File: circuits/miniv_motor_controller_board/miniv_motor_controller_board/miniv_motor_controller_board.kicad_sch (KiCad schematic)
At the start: 34 parts, among them J1 DC_in, J2 T200_ESC_power, J3 T200_ESC_signal, J4 Conn_EStop_Signal, Q1 2SC1815, Q2 2SC1815, U1 Teensy4.1, U2 TLP624, U3 TLP624

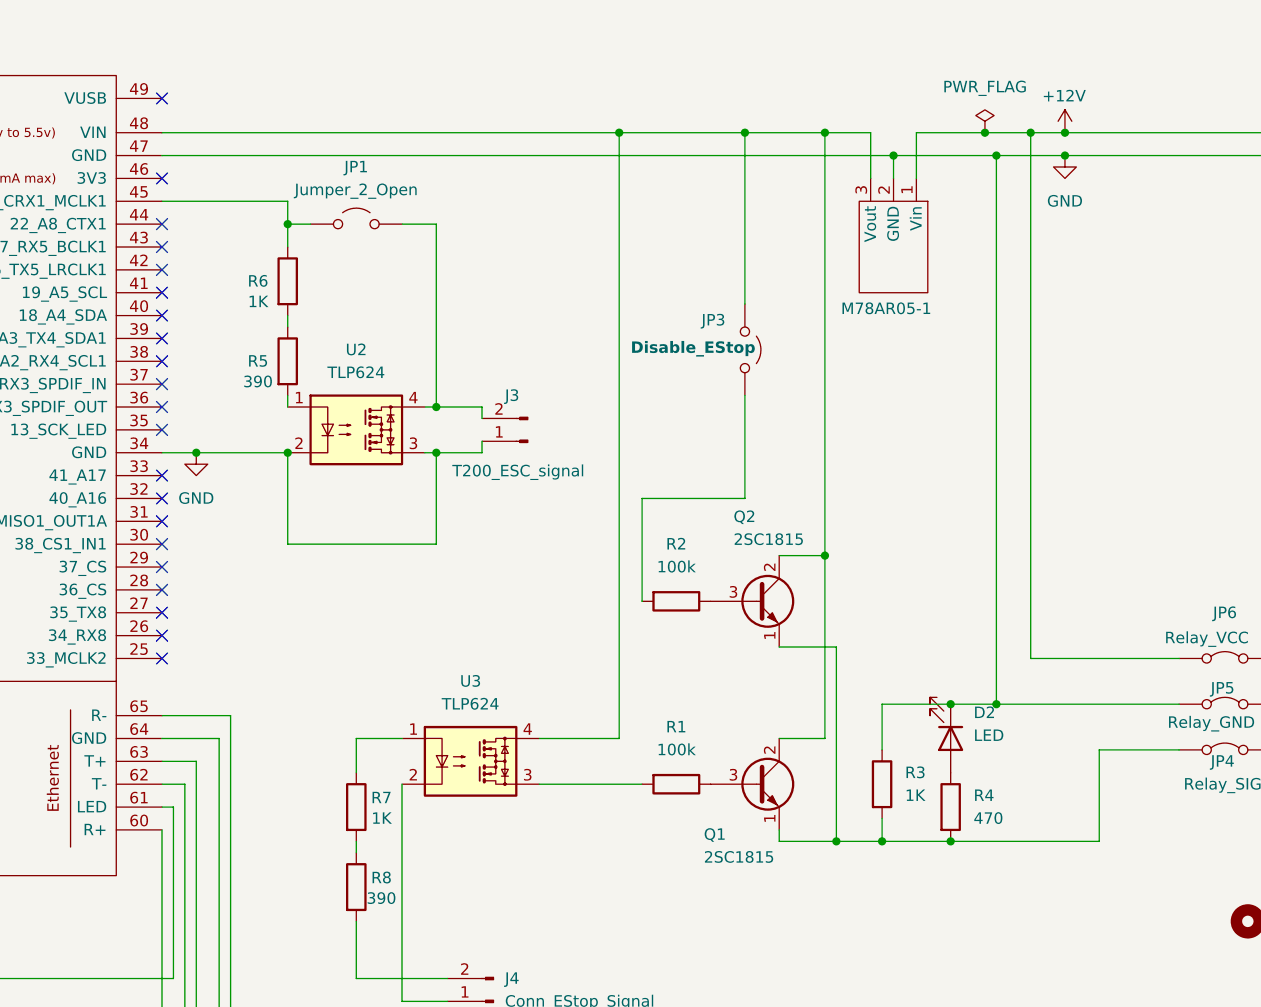
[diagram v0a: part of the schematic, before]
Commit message: add SS-12D00G3 and modify RJLD-260YC1
Signed-off-by: Masaya Kataoka <ms.kataoka@gmail.com>
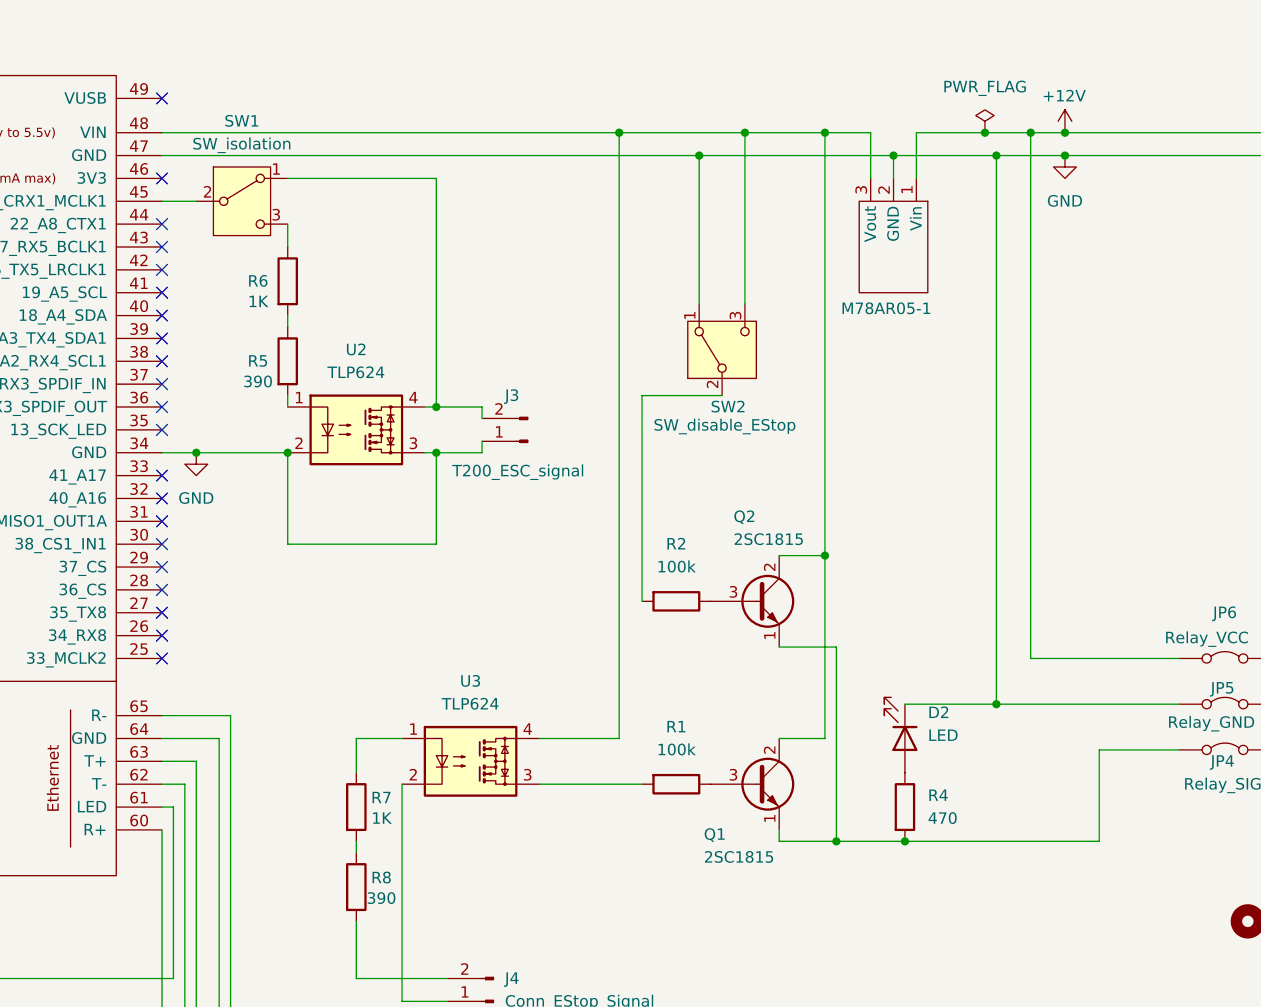
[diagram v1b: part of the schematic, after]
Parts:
- removed JP1: Jumper_2_Open, Connector_PinHeader_2.54mm:PinHeader_1x02_P2.54mm_Vertical, symbol Jumper:Jumper_2_Open
- removed JP3: Disable_EStop, Connector_PinHeader_2.54mm:PinHeader_1x02_P2.54mm_Vertical, symbol Jumper:Jumper_2_Open
- removed R3: 1K, Resistor_THT:R_Axial_DIN0207_L6.3mm_D2.5mm_P10.16mm_Horizontal, symbol Device:R
- added SW1: SW_isolation, SS-12D00G3:SS-12D00G3, symbol Switch:SW_SPDT
- added SW2: SW_disable_EStop, SS-12D00G3:SS-12D00G3, symbol Switch:SW_SPDT
- C1: footprint (none) -> Capacitor_THT:C_Disc_D5.1mm_W3.2mm_P5.00mm
- U5: footprint https://akizukidenshi.com/catalog/g/g129472/ -> RJLD-260YC1:RJLD-260YC1
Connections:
- net GND: now also SW2.1 (A)
- net at R6.1: now also SW1.3 (C); no longer U1.45 (23_A9_CRX1_MCLK1)
- net at J3.2 (Pin_2), U2.4: now also SW1.1 (A)
- net at M78AR05-1.3 (Vout), Q1.2 (C), Q2.2 (C)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: now also SW2.3 (C)
- net at R2.2: now also SW2.2 (B)
- net at U4. (VCC(CN1-1)): now also JP2.2 (B)
- new net: SW1.2 (B), U1.45 (23_A9_CRX1_MCLK1)
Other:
- moved on the sheet: D2, R4

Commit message: update board
Signed-off-by: Masaya Kataoka <ms.kataoka@gmail.com>
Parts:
- U1: footprint Teensy:Teensy41 -> Teensy_Custom:Teensy41
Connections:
- net GND: now also U1.1 (GND); no longer U1.47 (GND)
- net at U4. (VCC(CN1-1)): now also JP2.2 (B)
- net at SW1.2 (B): now also U1.33 (41_A17); no longer U1.45 (23_A9_CRX1_MCLK1)
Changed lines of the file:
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@@
 	)
 	(junction
-		(at 168.91 64.77)
+		(at 137.16 67.31)
 		(diameter 0)
 		(color 0 0 0 0)
 	)
 	(junction
-		(at 151.13 111.76)
+		(at 168.91 64.77)
 		(diameter 0)
 		(color 0 0 0 0)
 	)
 	(junction
-		(at 158.75 67.31)
+		(at 151.13 111.76)
 		(diameter 0)
 		(color 0 0 0 0)
 	)
 	(junction
-		(at 177.8 67.31)
+		(at 158.75 67.31)
 		(diameter 0)
 		(color 0 0 0 0)
 	)
 	(junction
-		(at 137.16 67.31)
+		(at 177.8 67.31)
 		(diameter 0)
 		(color 0 0 0 0)
@@
 	)
 	(no_connect
+		(at 77.47 72.39)
+	)
+	(no_connect
 		(at 21.59 69.85)
 	)
@@
 	)
 	(no_connect
-		(at 77.47 102.87)
+		(at 77.47 85.09)
 	)
 	(no_connect
-		(at 77.47 85.09)
+		(at 77.47 67.31)
 	)
 	(no_connect
@@
 	)
 	(no_connect
-		(at 21.59 64.77)
-	)
-	(no_connect
 		(at 21.59 118.11)
 	)
@@
 	(wire
 		(pts
-			(xy 78.74 158.75) (xy 78.74 139.7)
+			(xy 106.68 48.26) (xy 21.59 48.26)
 		)
 		(stroke
@@
 	(wire
 		(pts
-			(xy 77.47 180.34) (xy 46.99 180.34)
+			(xy 78.74 158.75) (xy 78.74 139.7)
 		)
 		(stroke
@@
 	(wire
 		(pts
-			(xy 152.4 143.51) (xy 160.02 143.51)
+			(xy 77.47 180.34) (xy 46.99 180.34)
 		)
 		(stroke
@@
 	(wire
 		(pts
-			(xy 107.95 100.33) (xy 113.03 100.33)
+			(xy 152.4 143.51) (xy 160.02 143.51)
 		)
 		(stroke
@@
 	(wire
 		(pts
-			(xy 156.21 64.77) (xy 156.21 69.85)
+			(xy 107.95 100.33) (xy 113.03 100.33)
 		)
 		(stroke
@@
 	(wire
 		(pts
-			(xy 77.47 72.39) (xy 81.28 72.39)
+			(xy 156.21 64.77) (xy 156.21 69.85)
 		)
 		(stroke
@@
 	(wire
 		(pts
+			(xy 85.09 102.87) (xy 77.47 102.87)
+		)
+		(stroke
+			(width 0)
+			(type default)
+		)
+	)
+	(wire
+		(pts
 			(xy 170.18 67.31) (xy 170.18 128.27)
 		)
@@
 	(wire
 		(pts
-			(xy 77.47 67.31) (xy 137.16 67.31)
+			(xy 81.28 82.55) (xy 85.09 82.55)
 		)
 		(stroke
@@
 	(wire
 		(pts
+			(xy 106.68 67.31) (xy 106.68 48.26)
+		)
+		(stroke
+			(width 0)
+			(type default)
+		)
+	)
+	(wire
+		(pts
 			(xy 177.8 64.77) (xy 260.35 64.77)
 		)
@@
 	(wire
 		(pts
+			(xy 81.28 72.39) (xy 81.28 82.55)
+		)
+		(stroke
+			(width 0)
+			(type default)
+		)
+	)
+	(wire
+		(pts
 			(xy 262.89 67.31) (xy 262.89 90.17)
 		)
@@
 	(wire
 		(pts
+			(xy 137.16 67.31) (xy 106.68 67.31)
+		)
+		(stroke
+			(width 0)
+			(type default)
+		)
+	)
+	(wire
+		(pts
 			(xy 91.44 85.09) (xy 91.44 86.36)
 		)
@@
 	(wire
 		(pts
+			(xy 21.59 48.26) (xy 21.59 64.77)
+		)
+		(stroke
+			(width 0)
+			(type default)
+		)
+	)
+	(wire
+		(pts
 			(xy 161.29 64.77) (xy 168.91 64.77)
 		)
@@
 	(wire
 		(pts
+			(xy 85.09 82.55) (xy 85.09 102.87)
+		)
+		(stroke
+			(width 0)
+			(type default)
+		)
+	)
+	(wire
+		(pts
 			(xy 62.23 176.53) (xy 72.39 176.53)
 		)
@@
 			)
 		)
-		(property "Footprint" "Teensy:Teensy41"
+		(property "Footprint" "Teensy_Custom:Teensy41"
 			(at 39.37 109.22 0)
 			(effects

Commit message: modify circuit
Signed-off-by: Masaya Kataoka <ms.kataoka@gmail.com>
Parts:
- removed Q1, Q2: 2SC1815, Package_TO_SOT_THT:TO-92_Inline, symbol Transistor_BJT:2SC1815
- removed SW1: SW_isolation, SS-12D00G3:SS-12D00G3, symbol Switch:SW_SPDT
- added SW1: SW_Push_DPDT, 2MD1-T2-B4-M2-Q-N:2MD1-T2-B4-M2-Q-N, symbol Switch:SW_Push_DPDT
- added U6: ~, Package_DIP:DIP-14_W7.62mm, symbol TC74HC32AP:TC74HC32AP
- R1, R2: value 100k -> 1k
- R4: value 470 -> 390
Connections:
- net GND: now also SW1.3 (C), U6.7 (GND); no longer J3.1 (Pin_1), U2.3
- net at U2.4: now also SW1.4 (A); no longer J3.2 (Pin_2)
- net at M78AR05-1.3 (Vout), SW2.3 (C), U1.48 (VIN)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: now also U6.14 (Vcc)
- net at R6.1: now also U1.33 (41_A17), SW1.6 (C)
- net at JP4.1 (A), R4.2: now also U6.3 (1Y)
- net at R2.1: now also U6.1 (1A)
- net at U4. (VCC(CN1-1)): now also JP2.2 (B)
- net at R1.1: now also U6.2 (1B)
- new net: SW1.1 (A), U2.3
- new net: J3.1 (Pin_1), SW1.2 (B)
- new net: J3.2 (Pin_2), SW1.5 (B)
- no-connect marks 61 -> 70
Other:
- moved on the sheet: D2, J3, R4, R5, R6, U2

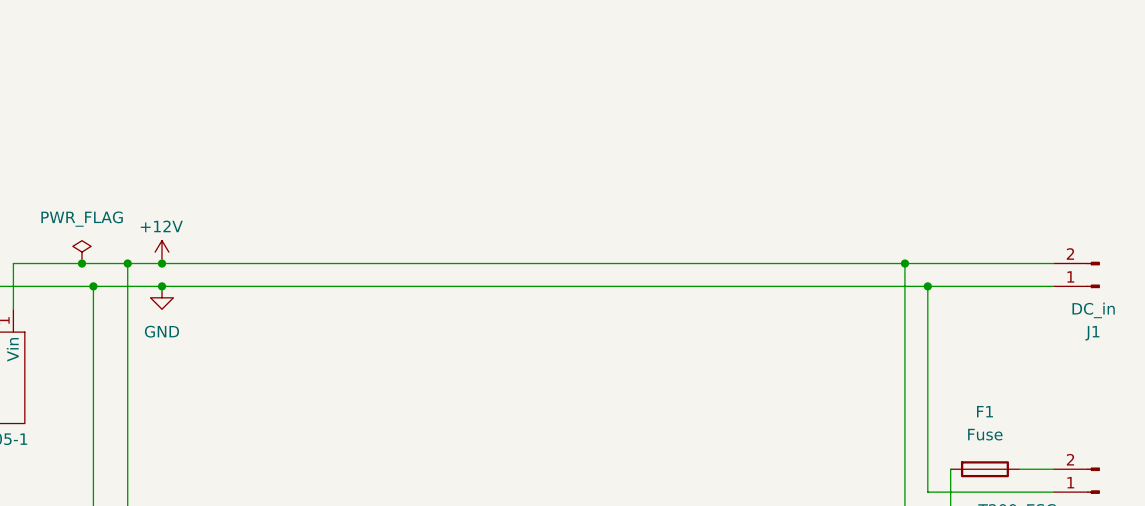
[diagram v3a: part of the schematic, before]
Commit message: add 12V DC/DC
Signed-off-by: Masaya Kataoka <ms.kataoka@gmail.com>
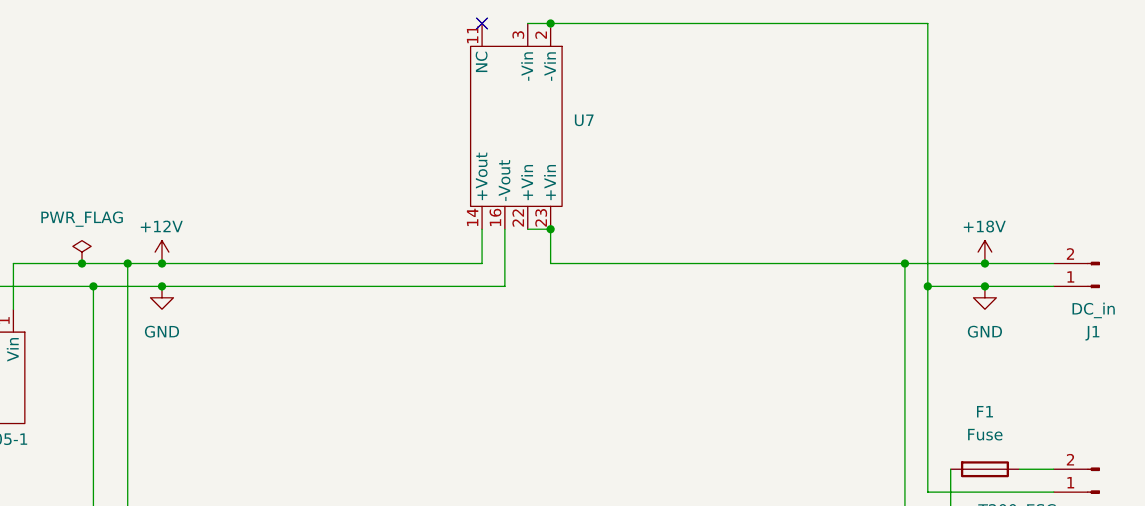
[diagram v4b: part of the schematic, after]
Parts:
- added U7: ~, symbol MIWI06-24S12:MIWI06-24S12
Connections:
- net +12V: now also U7.14 (+Vout); no longer J1.2 (Pin_2), JP7.1 (A)
- net GND: now also U7.16 (-Vout), U7.2 (-Vin), U7.3 (-Vin)
- net at U4. (VCC(CN1-1)): now also JP2.2 (B)
- new net +18V: J1.2 (Pin_2), JP7.1 (A), U7.22 (+Vin), U7.23 (+Vin)
- no-connect marks 70 -> 71

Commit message: update schematic
Signed-off-by: Masaya Kataoka <ms.kataoka@gmail.com>
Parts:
- U7: footprint (none) -> MIWI06-24S12:MIWI06-24S12
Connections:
- net at U4. (VCC(CN1-1)): now also JP2.2 (B)
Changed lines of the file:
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@@
-	)
-	(junction
-		(at 168.91 64.77)
-		(diameter 0)
-		(color 0 0 0 0)
 	)
 	(junction
@@
 	)
 	(junction
+		(at 236.22 64.77)
+		(diameter 0)
+		(color 0 0 0 0)
+	)
+	(junction
 		(at 173.99 64.77)
 		(diameter 0)
@@
 	(wire
 		(pts
-			(xy 168.91 64.77) (xy 173.99 64.77)
-		)
-		(stroke
-			(width 0)
-			(type default)
-		)
-	)
-	(wire
-		(pts
 			(xy 99.06 143.51) (xy 99.06 144.78)
 		)
@@
 	(wire
 		(pts
+			(xy 236.22 64.77) (xy 220.98 64.77)
+		)
+		(stroke
+			(width 0)
+			(type default)
+		)
+	)
+	(wire
+		(pts
 			(xy 100.33 102.87) (xy 82.55 102.87)
 		)
@@
 	(wire
 		(pts
-			(xy 260.35 64.77) (xy 220.98 64.77)
+			(xy 260.35 64.77) (xy 236.22 64.77)
 		)
 		(stroke
@@
 	(wire
 		(pts
-			(xy 161.29 64.77) (xy 168.91 64.77)
+			(xy 161.29 64.77) (xy 173.99 64.77)
 		)
 		(stroke
@@
 			(width 0)
 			(type default)
+		)
+	)
+	(symbol
+		(lib_id "power:PWR_FLAG")
+		(at 236.22 64.77 0)
+		(unit 1)
+		(exclude_from_sim no)
+		(in_bom yes)
+		(on_board yes)
+		(dnp no)
+		(fields_autoplaced yes)
+		(property "Reference" "#FLG02"
+			(at 236.22 62.865 0)
+			(effects
+				(font
+					(size 1.27 1.27)
+				)
+				(hide yes)
+			)
+		)
+		(property "Value" "PWR_FLAG"
+			(at 236.22 59.69 0)
+			(effects
+				(font
+					(size 1.27 1.27)
+				)
+			)
+		)
+		(property "Footprint" ""
+			(at 236.22 64.77 0)
+			(effects
+				(font
+					(size 1.27 1.27)
+				)
+				(hide yes)
+			)
+		)
+		(property "Datasheet" "~"
+			(at 236.22 64.77 0)
+			(effects
+				(font
+					(size 1.27 1.27)
+				)
+				(hide yes)
+			)
+		)
+		(property "Description" "Special symbol for telling ERC where power comes from"
+			(at 236.22 64.77 0)
+			(effects
+				(font
+					(size 1.27 1.27)
+				)
+				(hide yes)
+			)
+		)
+		(pin "1"
+		)
+		(instances
+			(project "miniv_motor_controller_board"
+				(path "/54ae4e30-07a3-4793-b6e1-7fe8564be1ba"
+					(reference "#FLG02")
+					(unit 1)
+				)
+			)
 		)
 	)
@@
 	)
 	(symbol
-		(lib_id "power:PWR_FLAG")
-		(at 168.91 64.77 0)
-		(unit 1)
-		(exclude_from_sim no)
-		(in_bom yes)
-		(on_board yes)
-		(dnp no)
-		(fields_autoplaced yes)
-		(property "Reference" "#FLG01"
-			(at 168.91 62.865 0)
-			(effects
-				(font
-					(size 1.27 1.27)
-				)
-				(hide yes)
-			)
-		)
-		(property "Value" "PWR_FLAG"
-			(at 168.91 59.69 0)
-			(effects
-				(font
-					(size 1.27 1.27)
-				)
-			)
-		)
-		(property "Footprint" ""
-			(at 168.91 64.77 0)
-			(effects
-				(font
-					(size 1.27 1.27)
-				)
-				(hide yes)
-			)
-		)
-		(property "Datasheet" "~"
-			(at 168.91 64.77 0)
-			(effects
-				(font
-					(size 1.27 1.27)
-				)
-				(hide yes)
-			)
-		)
-		(property "Description" "Special symbol for telling ERC where power comes from"
-			(at 168.91 64.77 0)
-			(effects
-				(font
-					(size 1.27 1.27)
-				)
-				(hide yes)
-			)
-		)
-		(pin "1"
-		)
-		(instances
-			(project ""
-				(path "/54ae4e30-07a3-4793-b6e1-7fe8564be1ba"
-					(reference "#FLG01")
-					(unit 1)
-				)
-			)
-		)
-	)
-	(symbol
 		(lib_id "RJLD-260YC1:RJLD-260YC1")
 		(at 33.02 176.53 0)
@@
 			)
 		)
-		(property "Footprint" ""
+		(property "Footprint" "MIWI06-24S12:MIWI06-24S12"
 			(at 217.17 49.53 0)
 			(effects

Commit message: re-design board
Signed-off-by: Masaya Kataoka <ms.kataoka@gmail.com>
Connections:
- net at SW1.1 (A): now also U1.34 (GND), U2.2; no longer U2.3
- net at U2.4: now also SW1.6 (C); no longer SW1.4 (A)
- net at R6.1, U1.33 (41_A17): now also SW1.4 (A); no longer SW1.6 (C)
- net at U4. (VCC(CN1-1)): now also JP2.2 (B)
- net +18V: no longer names the net of J1.2 (Pin_2), JP7.1 (A), U7.22 (+Vin), U7.23 (+Vin)
- net GND renamed GNDREF
- net GNDREF: no longer J1.1 (Pin_1), J2.1 (Pin_1), SW1.3 (C), U1.34 (GND), U2.2, U7.2 (-Vin), U7.3 (-Vin)
- new net: SW1.3 (C), U2.3
- new net GNDREF_Bat: J1.1 (Pin_1), J2.1 (Pin_1), U7.2 (-Vin), U7.3 (-Vin)

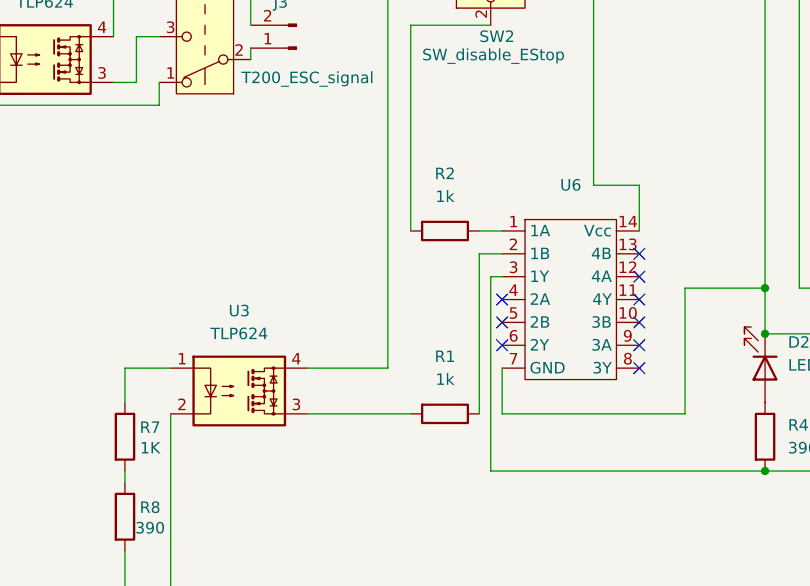
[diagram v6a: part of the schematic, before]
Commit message: remove R1/R2
Signed-off-by: Masaya Kataoka <ms.kataoka@gmail.com>
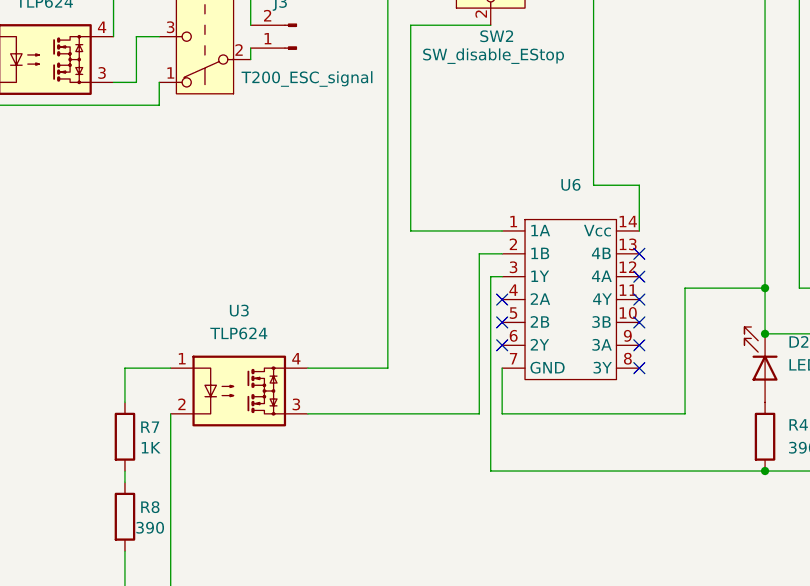
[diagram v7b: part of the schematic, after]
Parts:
- removed R1, R2: 1k, Resistor_THT:R_Axial_DIN0207_L6.3mm_D2.5mm_P10.16mm_Horizontal, symbol Device:R
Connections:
- net at SW2.2 (B): now also U6.1 (1A)
- net at U4. (VCC(CN1-1)): now also JP2.2 (B)
- net at U6.2 (1B): now also U3.3
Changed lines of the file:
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@@
+	(wire
+		(pts
+			(xy 130.81 116.84) (xy 140.97 116.84)
+		)
+		(stroke
+			(width 0)
+			(type default)
+		)
+	)
 	(wire
 		(pts
@@
 	(wire
 		(pts
-			(xy 140.97 116.84) (xy 138.43 116.84)
-		)
-		(stroke
-			(width 0)
-			(type default)
-		)
-	)
-	(wire
-		(pts
 			(xy 104.14 161.29) (xy 109.22 161.29)
 		)
@@
 	(wire
 		(pts
-			(xy 119.38 137.16) (xy 130.81 137.16)
+			(xy 119.38 137.16) (xy 138.43 137.16)
 		)
 		(stroke
@@
 	)
 	(symbol
-		(lib_id "Device:R")
-		(at 134.62 116.84 270)
-		(unit 1)
-		(exclude_from_sim no)
-		(in_bom yes)
-		(on_board yes)
-		(dnp no)
-		(fields_autoplaced yes)
-		(property "Reference" "R2"
-			(at 134.62 110.49 90)
-			(effects
-				(font
-					(size 1.27 1.27)
-				)
-			)
-		)
-		(property "Value" "1k"
-			(at 134.62 113.03 90)
-			(effects
-				(font
-					(size 1.27 1.27)
-				)
-			)
-		)
-		(property "Footprint" "Resistor_THT:R_Axial_DIN0207_L6.3mm_D2.5mm_P10.16mm_Horizontal"
-			(at 134.62 115.062 90)
-			(effects
-				(font
-					(size 1.27 1.27)
-				)
-				(hide yes)
-			)
-		)
-		(property "Datasheet" "https://akizukidenshi.com/catalog/g/g108535/"
-			(at 134.62 116.84 0)
-			(effects
-				(font
-					(size 1.27 1.27)
-				)
-				(hide yes)
-			)
-		)
-		(property "Description" "Resistor"
-			(at 134.62 116.84 0)
-			(effects
-				(font
-					(size 1.27 1.27)
-				)
-				(hide yes)
-			)
-		)
-		(pin "2"
-		)
-		(pin "1"
-		)
-		(instances
-			(project "miniv_motor_controller_board"
-				(path "/54ae4e30-07a3-4793-b6e1-7fe8564be1ba"
-					(reference "R2")
-					(unit 1)
-				)
-			)
-		)
-	)
-	(symbol
 		(lib_id "Mechanical:MountingHole")
 		(at 233.68 152.4 0)
@@
 					(unit 1)
 				)
-			)
-		)
-	)
-	(symbol
-		(lib_id "Device:R")
-		(at 134.62 137.16 270)
-		(unit 1)
-		(exclude_from_sim no)
-		(in_bom yes)
-		(on_board yes)
-		(dnp no)
-		(fields_autoplaced yes)
-		(property "Reference" "R1"
-			(at 134.62 130.81 90)
-			(effects
-				(font
-					(size 1.27 1.27)
-				)
-			)
-		)
-		(property "Value" "1k"
-			(at 134.62 133.35 90)
-			(effects
-				(font
-					(size 1.27 1.27)
-				)
-			)
-		)
-		(property "Footprint" "Resistor_THT:R_Axial_DIN0207_L6.3mm_D2.5mm_P10.16mm_Horizontal"
-			(at 134.62 135.382 90)
-			(effects
-				(font
-					(size 1.27 1.27)
-				)
-				(hide yes)
-			)
-		)
-		(property "Datasheet" "https://akizukidenshi.com/catalog/g/g108535/"
-			(at 134.62 137.16 0)
-			(effects
-				(font
-					(size 1.27 1.27)
-				)
-				(hide yes)
-			)
-		)
-		(property "Description" "Resistor"
-			(at 134.62 137.16 0)
-			(effects
-				(font
-					(size 1.27 1.27)
-				)
-				(hide yes)
-			)
-		)
-		(pin "2"
-		)
-		(pin "1"
-		)
-		(instances
-			(project ""
-				(path "/54ae4e30-07a3-4793-b6e1-7fe8564be1ba"
-					(reference "R1")
-					(unit 1)
-				)
